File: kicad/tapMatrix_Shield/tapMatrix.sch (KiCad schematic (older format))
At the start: 4 parts

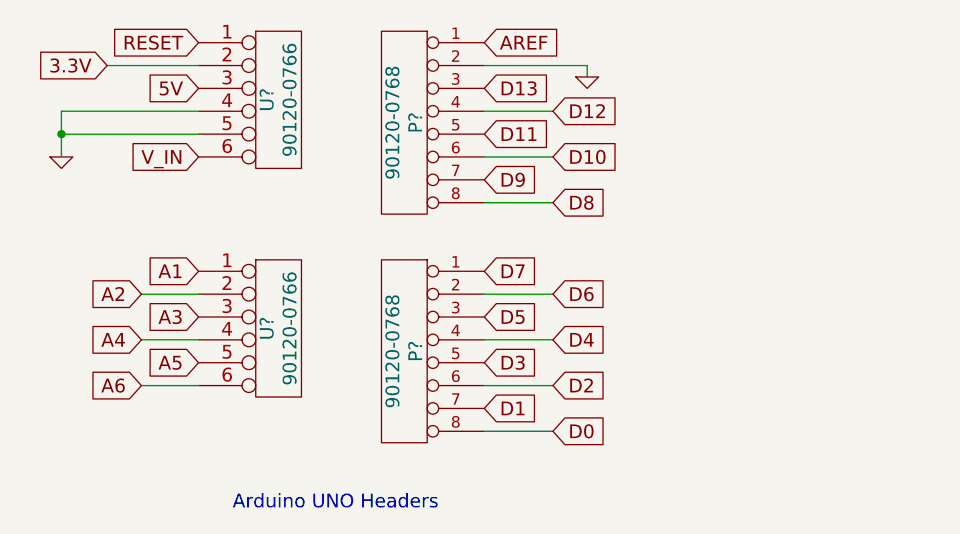
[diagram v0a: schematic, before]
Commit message: Added ZIF socket, created component library, fixed Arduino headers
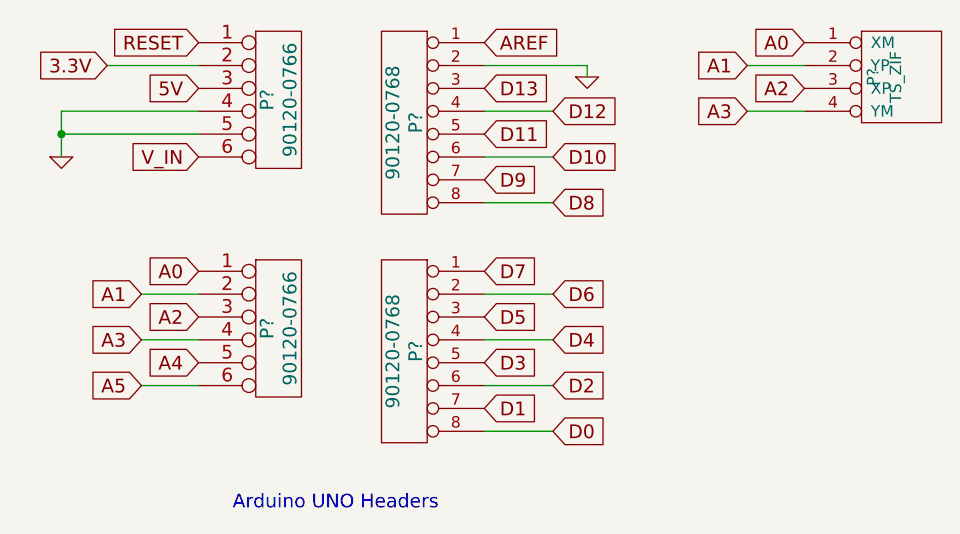
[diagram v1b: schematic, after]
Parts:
- added P?: TS_ZIF, symbol TS_ZIF
- gave numbers to parts that had none: 1
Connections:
- net A6 is gone; now on net A5: P?.6
- net A1: now also P?.2, P?.2 (YP); no longer P?.1
- net A2: now also P?.3, P?.3 (XP); no longer P?.2
- net A3: now also P?.4, P?.4 (YM); no longer P?.3
- net A4: now also P?.5; no longer P?.4
- net A5: no longer P?.5
- new net A0: P?.1, P?.1 (XM)
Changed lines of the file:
@@
 LIBS:contrib
 LIBS:valves
+LIBS:tapMatrix
 LIBS:tapMatrix-cache
 EELAYER 24 0
@@
 $EndDescr
 $Comp
-L CONN_6 U?
+L CONN_6 P?
 U 1 1 53F232C2
 P 1850 1450
-F 0 "U?" V 1800 1450 60  0000 C CNN
+F 0 "P?" V 1800 1450 60  0000 C CNN
 F 1 "90120-0766" V 1900 1450 60  0000 C CNN
 F 2 "" H 1850 1450 60  0000 C CNN
@@
 Connection ~ 900  1600
 $Comp
-L CONN_6 U?
+L CONN_6 P?
 U 1 1 53F2345E
 P 1850 2450
-F 0 "U?" V 1800 2450 60  0000 C CNN
+F 0 "P?" V 1800 2450 60  0000 C CNN
 F 1 "90120-0766" V 1900 2450 60  0000 C CNN
 F 2 "" H 1850 2450 60  0000 C CNN
@@
 $EndComp
 Text GLabel 1500 2200 0    60   Input ~ 0
+A0
+Text GLabel 1250 2300 0    60   Input ~ 0
 A1
-Text GLabel 1250 2300 0    60   Input ~ 0
+Text GLabel 1500 2400 0    60   Input ~ 0
 A2
-Text GLabel 1500 2400 0    60   Input ~ 0
+Text GLabel 1250 2500 0    60   Input ~ 0
 A3
-Text GLabel 1250 2500 0    60   Input ~ 0
+Text GLabel 1500 2600 0    60   Input ~ 0
 A4
-Text GLabel 1500 2600 0    60   Input ~ 0
+Text GLabel 1250 2700 0    60   Input ~ 0
 A5
-Text GLabel 1250 2700 0    60   Input ~ 0
-A6
 Wire Wire Line
 	1500 2300 1250 2300
@@
 Text Notes 2550 3250 2    60   ~ 0
 Arduino UNO Headers
+$Comp
+L TS_ZIF P?
+U 1 1 53F23B9F
+P 4500 1350
+F 0 "P?" V 4450 1350 50  0000 C CNN
+F 1 "TS_ZIF" V 4550 1350 50  0000 C CNN
+F 2 "" H 4500 1350 60  0000 C CNN
+F 3 "" H 4500 1350 60  0000 C CNN
+	1    4500 1350
+	1    0    0    -1
+$EndComp
+Text GLabel 4150 1200 0    60   Input ~ 0
+A0
+Text GLabel 3900 1300 0    60   Input ~ 0
+A1
+Text GLabel 4150 1400 0    60   Input ~ 0
+A2
+Text GLabel 3900 1500 0    60   Input ~ 0
+A3
+Wire Wire Line
+	3900 1500 4150 1500
+Wire Wire Line
+	3900 1300 4150 1300
 $EndSCHEMATC

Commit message: add led matrix header, microsd component, update libraries
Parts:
- added P?: LED_MATRIX_HDR, symbol LED_MATRIX_HDR
- added U?: SD_CARD, symbol SD_CARD
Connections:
- net labels added: CS, MOSI, SCLK
- wire segments 18 -> 41
- no-connect marks 0 -> 7
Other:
- note added: "LED Matrix Header"
- note added: "MicroSD Card Socket"
- note added: "Touchscreen ZIF Socket"
- moved on the sheet: P?
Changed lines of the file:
@@
 L TS_ZIF P?
 U 1 1 53F23B9F
-P 4500 1350
-F 0 "P?" V 4450 1350 50  0000 C CNN
-F 1 "TS_ZIF" V 4550 1350 50  0000 C CNN
-F 2 "" H 4500 1350 60  0000 C CNN
-F 3 "" H 4500 1350 60  0000 C CNN
-	1    4500 1350
+P 5300 2550
+F 0 "P?" H 5350 2850 50  0000 C CNN
+F 1 "TS_ZIF" V 5500 2550 50  0000 C CNN
+F 2 "" H 5300 2550 60  0000 C CNN
+F 3 "" H 5300 2550 60  0000 C CNN
+	1    5300 2550
 	1    0    0    -1
 $EndComp
-Text GLabel 4150 1200 0    60   Input ~ 0
+Text GLabel 4950 2400 0    60   Input ~ 0
 A0
-Text GLabel 3900 1300 0    60   Input ~ 0
+Text GLabel 4700 2500 0    60   Input ~ 0
 A1
-Text GLabel 4150 1400 0    60   Input ~ 0
+Text GLabel 4950 2600 0    60   Input ~ 0
 A2
-Text GLabel 3900 1500 0    60   Input ~ 0
+Text GLabel 4700 2700 0    60   Input ~ 0
 A3
 Wire Wire Line
-	3900 1500 4150 1500
+	4700 2700 4950 2700
 Wire Wire Line
-	3900 1300 4150 1300
+	4700 2500 4950 2500
+$Comp
+L LED_MATRIX_HDR P?
+U 1 1 53F2DDF1
+P 7650 2100
+F 0 "P?" H 7650 2850 60  0000 C CNN
+F 1 "LED_MATRIX_HDR" H 7650 1400 50  0000 C CNN
+F 2 "" H 7650 2100 60  0000 C CNN
+F 3 "" H 7650 2100 60  0000 C CNN
+	1    7650 2100
+	1    0    0    -1
+$EndComp
+Text GLabel 7000 1550 0    60   Input ~ 0
+D0
+NoConn ~ 7000 1700
+NoConn ~ 7000 1850
+NoConn ~ 7000 2150
+NoConn ~ 8250 2150
+NoConn ~ 8250 1700
+$Comp
+L GND #PWR?
+U 1 1 53F2DE59
+P 6750 2150
+F 0 "#PWR?" H 6750 2150 30  0001 C CNN
+F 1 "GND" H 6750 2080 30  0001 C CNN
+F 2 "" H 6750 2150 60  0000 C CNN
+F 3 "" H 6750 2150 60  0000 C CNN
+	1    6750 2150
+	1    0    0    -1
+$EndComp
+Wire Wire Line
+	-69150 -60200 -69350 -60200
+Wire Wire Line
+	-69350 -60200 -69350 -60100
+Wire Wire Line
+	-69150 -60000 -69150 -59800
+Connection ~ -69150 -59900
+Text GLabel 7000 2450 0    60   Input ~ 0
+5V
+Text GLabel 8550 1550 2    60   Input ~ 0
+D1
+Text GLabel 8250 2000 2    60   Input ~ 0
+D6
+Text GLabel 8550 1850 2    60   Input ~ 0
+D7
+Wire Wire Line
+	-68100 -60200 -68350 -60200
+Wire Wire Line
+	-68100 -60500 -68350 -60500
+Wire Wire Line
+	-68350 -60000 -68350 -59800
+Connection ~ -68350 -59900
+$Comp
+L GND #PWR?
+U 1 1 53F2E04E
+P 8650 2600
+F 0 "#PWR?" H 8650 2600 30  0001 C CNN
+F 1 "GND" H 8650 2530 30  0001 C CNN
+F 2 "" H 8650 2600 60  0000 C CNN
+F 3 "" H 8650 2600 60  0000 C CNN
+	1    8650 2600
+	1    0    0    -1
+$EndComp
+Wire Wire Line
+	-68000 -59850 -68000 -59900
+Wire Wire Line
+	-68000 -59900 -68350 -59900
+Text Notes 5500 3250 2    60   ~ 0
+Touchscreen ZIF Socket
+Text Notes 8000 3250 2    60   ~ 0
+LED Matrix Header
+$Comp
+L SD_CARD U?
+U 1 1 53F2E748
+P 10650 2050
+F 0 "U?" H 10700 2750 60  0000 C CNN
+F 1 "SD_CARD" H 10650 1350 60  0000 C CNN
+F 2 "" H 10650 2250 60  0000 C CNN
+F 3 "" H 10650 2250 60  0000 C CNN
+	1    10650 2050
+	1    0    0    -1
+$EndComp
+Wire Wire Line
+	7000 2000 6750 2000
+Wire Wire Line
+	6750 2000 6750 2150
+Wire Wire Line
+	7000 2300 7000 2600
+Connection ~ 7000 2450
+Wire Wire Line
+	8550 1850 8250 1850
+Wire Wire Line
+	8550 1550 8250 1550
+Wire Wire Line
+	8250 2300 8250 2600
+Connection ~ 8250 2450
+Wire Wire Line
+	8250 2450 8650 2450
+Wire Wire Line
+	8650 2450 8650 2600
+Text Notes 11050 3250 2    60   ~ 0
+MicroSD Card Socket
+NoConn ~ 9950 1550
+Text GLabel 9950 1750 0    60   Input ~ 0
+CS
+Text GLabel 9950 1950 0    60   Input ~ 0
+MOSI
+Text GLabel 9950 2150 0    60   Input ~ 0
+3.3V
+Text GLabel 11350 1550 2    60   Input ~ 0
+SCLK
+$Comp
+L GND #PWR?
+U 1 1 53F3050A
+P 11800 2650
+F 0 "#PWR?" H 11800 2650 30  0001 C CNN
+F 1 "GND" H 11800 2580 30  0001 C CNN
+F 2 "" H 11800 2650 60  0000 C CNN
+F 3 "" H 11800 2650 60  0000 C CNN
+	1    11800 2650
+	1    0    0    -1
+$EndComp
+Text GLabel 11350 1950 2    60   Input ~ 0
+D12
+NoConn ~ 11350 2150
+Wire Wire Line
+	11350 1750 11800 1750
+Wire Wire Line
+	11800 1750 11800 2650
+Wire Wire Line
+	11350 2350 11800 2350
+Connection ~ 11800 2350
+Wire Wire Line
+	11350 2550 11800 2550
+Connection ~ 11800 2550
+$Comp
+L GND #PWR?
+U 1 1 53F30748
+P 9800 2650
+F 0 "#PWR?" H 9800 2650 30  0001 C CNN
+F 1 "GND" H 9800 2580 30  0001 C CNN
+F 2 "" H 9800 2650 60  0000 C CNN
+F 3 "" H 9800 2650 60  0000 C CNN
+	1    9800 2650
+	1    0    0    -1
+$EndComp
+Wire Wire Line
+	9950 2350 9800 2350
+Wire Wire Line
+	9800 2350 9800 2650
+Wire Wire Line
+	9950 2550 9800 2550
+Connection ~ 9800 2550
 $EndSCHEMATC

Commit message: improved headers, replaced global labels with local labels
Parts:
- added JP?: 6_PIN_1, symbol 6_PIN_1
- added JP?: 6_PIN_2, symbol 6_PIN_2
- added JP?: 8_PIN_1, symbol 8_PIN_1
- added JP?: 8_PIN_2, symbol 8_PIN_2
- added R?: 10K, symbol R
- added U? (x4): 74LS125, symbol 74LS125
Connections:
- net labels added: +3.3V, +5V, MATRIX_CLK, MATRIX_CS, MATRIX_DATA, MATRIX_WR, MISO, XM, XP, YM, YP
- wire segments 41 -> 65
- no-connect marks 7 -> 11
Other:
- note added: "is this D10 or D11? check into this...\nshould be MMC_CS. confirm that D10 is jumpered to pin 5"
- note added: "this needs to be sorted out when not sleepy"

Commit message: confirm and revise quad-buffer and microsd schematic details
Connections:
- net labels added: SCK, SD_CS
- wire segments 65 -> 74
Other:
- note added: "Quad-Buffer"
- note removed: "is this D10 or D11? check into this...\nshould be MMC_CS. confirm that D10 is jumpered to pin 5"
- note removed: "this needs to be sorted out when not sleepy"

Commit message: add 3.3V power supply, DAC, AMP, and Speaker Out
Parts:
- added C? (x5): 0.1uF, symbol C
- added C?: 0.01uF, symbol C
- added C? (x3): 100uF/6V, symbol C
- added P?: SPKR, symbol CONN_2
- added R?: 100K, symbol R
- added R?: 1.5K, symbol R
- added RV?: POT, symbol POT
- added U?: MCP4921-E/SN, SO8, symbol MCP4921-E/SN
- added U? (x2): TL072, symbol TL072
- added U?: APE8865N-33-HF-3, SOT-23, symbol APE8865N-33-HF-3
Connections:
- net labels added: DAC_CS, DAC_DI, DAC_LAT, DAC_SCK
- wire segments 74 -> 110
- no-connect marks 11 -> 12
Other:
- note added: "3.3V POWER SUPLY & BYPASS"
- note added: "AMP"
- note added: "DAC"
- note added: "VOLUME"

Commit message: add real time clock to schematic
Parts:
- added BT?: BATTERY, symbol BATTERY
- added IC?: DS1307, symbol DS1307
- added R? (x2): R, symbol R
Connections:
- net labels added: I2C_SCL, I2C_SDA
- wire segments 110 -> 126
- no-connect marks 12 -> 15

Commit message: schematic edits to resolve error checking messages
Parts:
- removed P? (x2): 90120-0766, symbol CONN_6
- removed P? (x2): 90120-0768, symbol CONN_8
- C1, C2, C3, C4, C5, C6, C7, C8, C9: renamed from C?; footprint (none) -> Capacitors_SMD:c_0603
- IC1: renamed from IC?; footprint (none) -> Housings_SOIC:SOIC-8_N
- JP1, JP2: renamed from JP?; footprint (none) -> Pin_Headers:Pin_Header_Straight_1x06
- JP3, JP4: renamed from JP?; footprint (none) -> Pin_Headers:Pin_Header_Straight_1x08
- P7: renamed from P?; footprint (none) -> Pin_Headers:Pin_Header_Straight_1x02
- R1, R2, R3, R4, R5: renamed from R?; footprint (none) -> Resistors_SMD:R_0603
- U1: renamed from U?; footprint SOT-23 -> SMD_Packages:SOT-23
- U2: renamed from U?; footprint SO8 -> SMD_Packages:SOIC-8-N
- U3: renamed from U?; footprint (none) -> SMD_Packages:SOIC-14_W
- U4: renamed from U?; footprint (none) -> SMD_Packages:SOIC-14_N
- gave numbers to parts that had none: 5
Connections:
- net labels removed: 3.3V, 5V, A0, A1, A2, A3, A4, A5, AREF, D0, D1, D10, D11, D12, D13, D2, D3, D4, D5, D6, D7, D8, D9, RESET, V_IN
- wire segments 126 -> 133
- no-connect marks 15 -> 19
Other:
- note added: "REAL TIME CLOCK"

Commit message: created power and signal netclasses, updated design rules for oshpark
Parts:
- BT1: footprint (none) -> tapmatrix:CR2032
- P5: footprint (none) -> tapmatrix:SFW4R­5STE1LF
- P6: footprint (none) -> tapmatrix:5103310­-3
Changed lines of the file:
@@
 F 0 "P5" H 5350 2850 50  0000 C CNN
 F 1 "TS_ZIF" V 5500 2550 50  0000 C CNN
-F 2 "" H 5300 2550 60  0001 C CNN
+F 2 "tapmatrix:SFW4R­5STE1LF" H 5300 2550 60  0001 C CNN
 F 3 "" H 5300 2550 60  0000 C CNN
 	1    5300 2550
@@
 F 0 "P6" H 7650 2850 60  0000 C CNN
 F 1 "LED_MATRIX_HDR" H 7650 1400 50  0000 C CNN
-F 2 "" H 7650 2100 60  0001 C CNN
-F 3 "" H 7650 2100 60  0000 C CNN
+F 2 "tapmatrix:5103310­-3" H 7650 2100 60  0001 C CNN
+F 3 "http://www.te.com/commerce/DocumentDelivery/DDEController?Action=srchrtrv&DocNm=5103310&DocType=Customer+Drawing&DocLang=English" H 7650 2100 60  0001 C CNN
 	1    7650 2100
 	1    0    0    -1
@@
 F 0 "BT1" H 1650 7900 50  0000 C CNN
 F 1 "BATTERY" H 1650 7510 50  0000 C CNN
-F 2 "" H 1650 7700 60  0001 C CNN
+F 2 "tapmatrix:CR2032" H 1650 7700 60  0001 C CNN
 F 3 "" H 1650 7700 60  0000 C CNN
 	1    1650 7700
